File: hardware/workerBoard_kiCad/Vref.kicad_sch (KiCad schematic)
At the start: 10 parts, among them U3 ADR435BRZ, U4 REG103UA-5, U5 ADP7118ARDZ-3.3-R7, U6 ADR4540BRZ

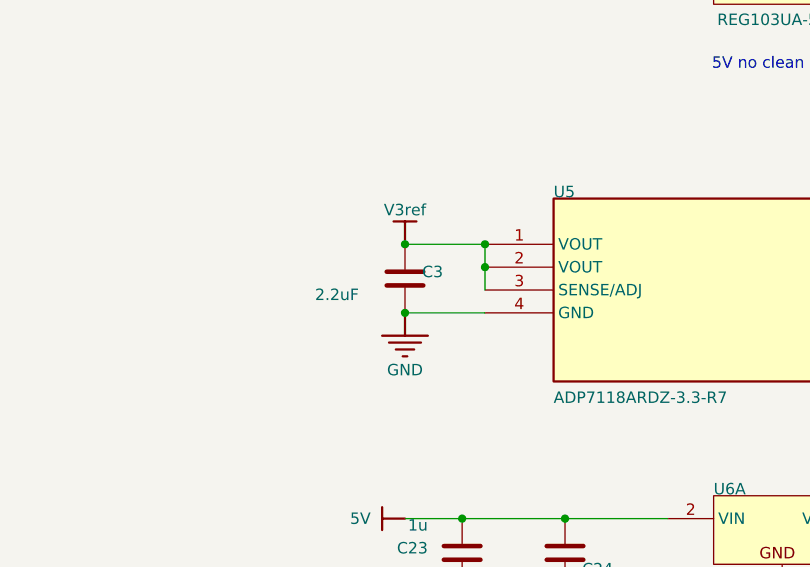
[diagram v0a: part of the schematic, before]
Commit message: Changed worker board layout V2
Removed micro-vias, used only two layers, changed connectors and generally re-worked the worker board
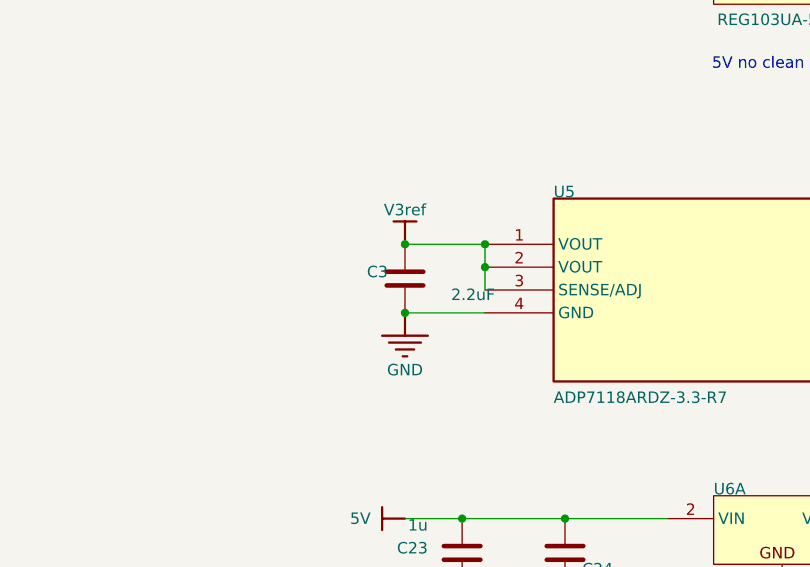
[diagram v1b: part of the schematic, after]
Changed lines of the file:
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@@
     (pin "4")
     (pin "6")
+    (pin "1")
+    (pin "3")
+    (pin "5")
+    (pin "7")
+    (pin "8")
   )
   (symbol (lib_id "Vref-altium-import:GND") (at 135.89 116.84 0) (unit 1)
@@
       (effects (font (size 1.27 1.27)) (justify left bottom) hide)
     )
+    (pin "2")
+    (pin "4")
+    (pin "5")
+    (pin "6")
+    (pin "7")
     (pin "1")
     (pin "3")
@@
     (pin "")
   )
-  (symbol (lib_id "Device:C") (at 135.89 113.03 0) (unit 1)
-    (in_bom yes) (on_board yes)
-    (property "Reference" "C3" (id 0) (at 137.795 113.03 0)
-      (effects (font (size 1.27 1.27)) (justify left bottom))
-    )
-    (property "Value" "2.2uF" (id 1) (at 125.89 115.57 0)
-      (effects (font (size 1.27 1.27)) (justify left bottom))
-    )
-    (property "Footprint" "lib:CAPC1608X90" (id 2) (at 136.8552 116.84 0)
+  (symbol (lib_id "Device:C") (at 135.89 113.03 0) (mirror y) (unit 1)
+    (in_bom yes) (on_board yes)
+    (property "Reference" "C3" (id 0) (at 133.985 113.03 0)
+      (effects (font (size 1.27 1.27)) (justify left bottom))
+    )
+    (property "Value" "2.2uF" (id 1) (at 145.89 115.57 0)
+      (effects (font (size 1.27 1.27)) (justify left bottom))
+    )
+    (property "Footprint" "lib:CAPC1608X90" (id 2) (at 134.9248 116.84 0)
       (effects (font (size 1.27 1.27)) hide)
     )
@@
       (effects (font (size 1.27 1.27)) hide)
     )
-    (property "PACKAGE" "None" (id 4) (at 133.985 107.442 0)
-      (effects (font (size 1.27 1.27)) (justify left bottom) hide)
-    )
-    (property "AVAILABILITY" "Unavailable" (id 5) (at 133.985 107.442 0)
-      (effects (font (size 1.27 1.27)) (justify left bottom) hide)
-    )
-    (property "ALTIUM_VALUE" "*" (id 6) (at 133.985 107.442 0)
-      (effects (font (size 1.27 1.27)) (justify left bottom) hide)
-    )
-    (property "MP" "F981C225MMA" (id 7) (at 133.985 107.442 0)
-      (effects (font (size 1.27 1.27)) (justify left bottom) hide)
-    )
-    (property "PRICE" "None" (id 8) (at 133.985 107.442 0)
-      (effects (font (size 1.27 1.27)) (justify left bottom) hide)
-    )
-    (property "MF" "{'manufacturer': u'AVX'}" (id 9) (at 133.985 107.442 0)
-      (effects (font (size 1.27 1.27)) (justify left bottom) hide)
-    )
-    (property "COMPONENT TYPE" "Standard" (id 10) (at 125.89 107.442 0)
-      (effects (font (size 1.27 1.27)) (justify left bottom) hide)
-    )
-    (property "DESIGN ITEM ID" "F981C225MMA" (id 11) (at 125.89 107.442 0)
-      (effects (font (size 1.27 1.27)) (justify left bottom) hide)
-    )
-    (property "PIN COUNT" "2" (id 12) (at 125.89 107.442 0)
-      (effects (font (size 1.27 1.27)) (justify left bottom) hide)
-    )
-    (property "SOURCE" "workerBoard.SCHLIB" (id 13) (at 125.89 107.442 0)
+    (property "PACKAGE" "None" (id 4) (at 137.795 107.442 0)
+      (effects (font (size 1.27 1.27)) (justify left bottom) hide)
+    )
+    (property "AVAILABILITY" "Unavailable" (id 5) (at 137.795 107.442 0)
+      (effects (font (size 1.27 1.27)) (justify left bottom) hide)
+    )
+    (property "ALTIUM_VALUE" "*" (id 6) (at 137.795 107.442 0)
+      (effects (font (size 1.27 1.27)) (justify left bottom) hide)
+    )
+    (property "MP" "F981C225MMA" (id 7) (at 137.795 107.442 0)
+      (effects (font (size 1.27 1.27)) (justify left bottom) hide)
+    )
+    (property "PRICE" "None" (id 8) (at 137.795 107.442 0)
+      (effects (font (size 1.27 1.27)) (justify left bottom) hide)
+    )
+    (property "MF" "{'manufacturer': u'AVX'}" (id 9) (at 137.795 107.442 0)
+      (effects (font (size 1.27 1.27)) (justify left bottom) hide)
+    )
+    (property "COMPONENT TYPE" "Standard" (id 10) (at 145.89 107.442 0)
+      (effects (font (size 1.27 1.27)) (justify left bottom) hide)
+    )
+    (property "DESIGN ITEM ID" "F981C225MMA" (id 11) (at 145.89 107.442 0)
+      (effects (font (size 1.27 1.27)) (justify left bottom) hide)
+    )
+    (property "PIN COUNT" "2" (id 12) (at 145.89 107.442 0)
+      (effects (font (size 1.27 1.27)) (justify left bottom) hide)
+    )
+    (property "SOURCE" "workerBoard.SCHLIB" (id 13) (at 145.89 107.442 0)
       (effects (font (size 1.27 1.27)) (justify left bottom) hide)
     )
@@
     (pin "6")
     (pin "7")
+    (pin "1")
+    (pin "3")
+    (pin "8")
   )
   (symbol (lib_id "Vref-altium-import:5V") (at 198.12 111.76 90) (unit 1)
@@
       (effects (font (size 1.27 1.27)) (justify left bottom) hide)
     )
+    (pin "2")
+    (pin "4")
+    (pin "6")
     (pin "1")
     (pin "3")

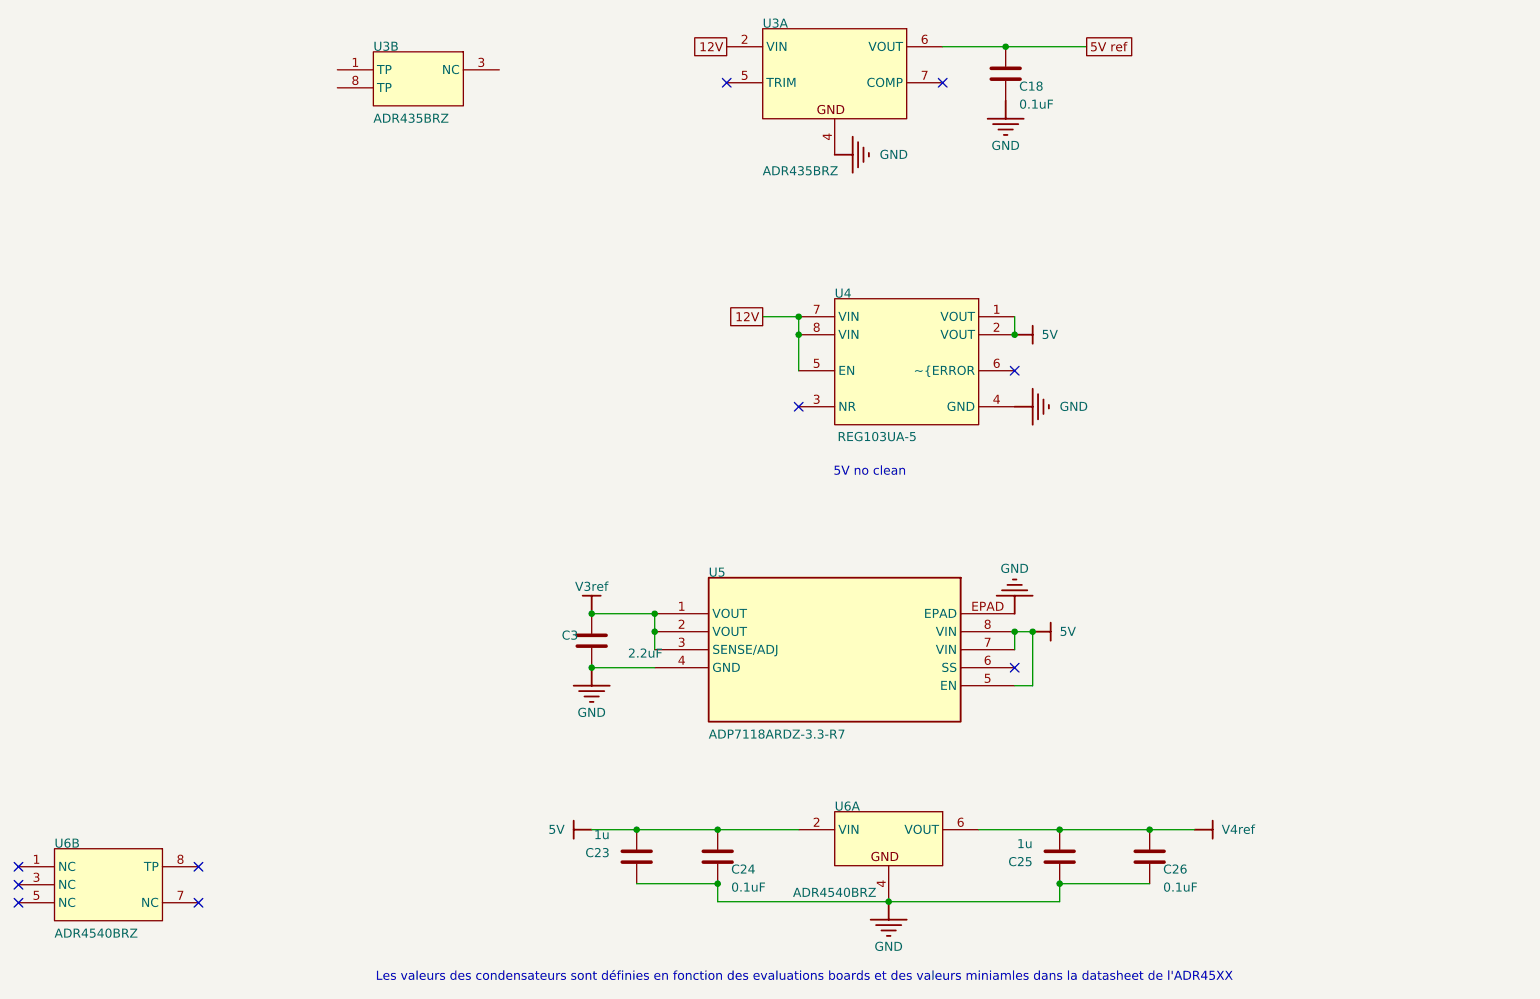
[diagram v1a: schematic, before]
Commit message: Fixed DRC violations
Fixed DRC violations based on missing footprints. Should review THVD8000 foot print as it had to be changed from 'missing' footprint import. This version passes all DRC checks. Net clearance was changed to 0.127 mm (4mill) otherwise the SOT-23 pads were failling DRC
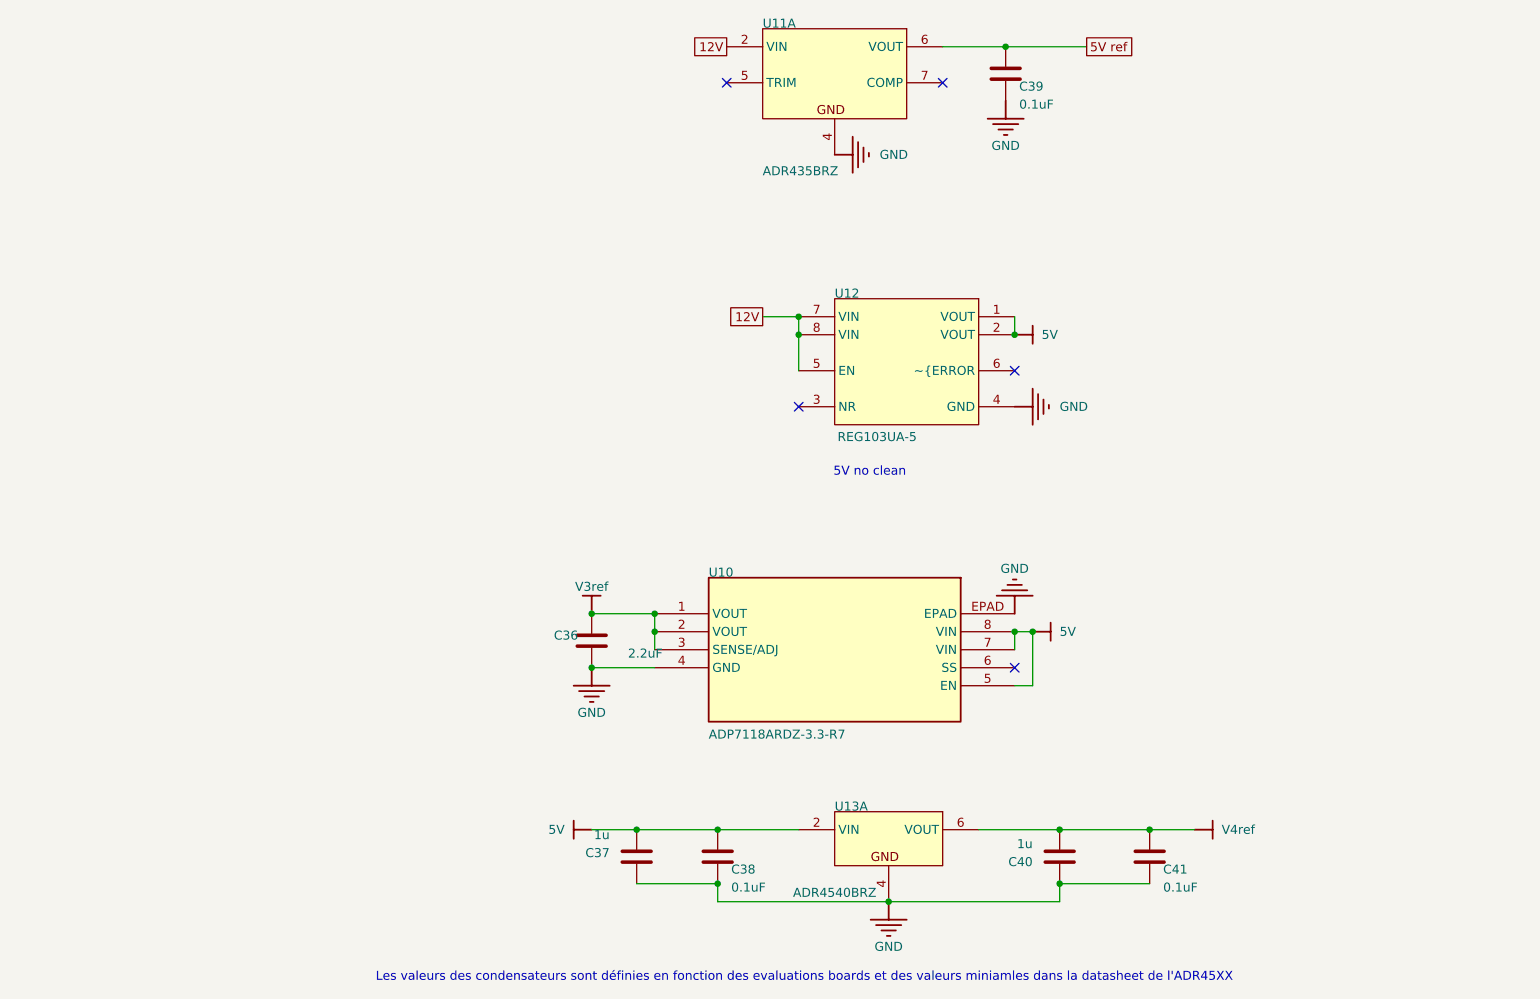
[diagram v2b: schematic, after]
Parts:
- removed unit 2 of U3
- removed unit 2 of U6
- U13: renamed from U6; footprint lib:ADI-R-8_M -> GIGUL-IMPORT:ADI-R-8_M
- renumbered C3 to C36, C23 to C37, C24 to C38, C18 to C39, C25 to C40, C26 to C41, U5 to U10, U3 to U11, U4 to U12
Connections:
- no-connect marks 10 -> 5

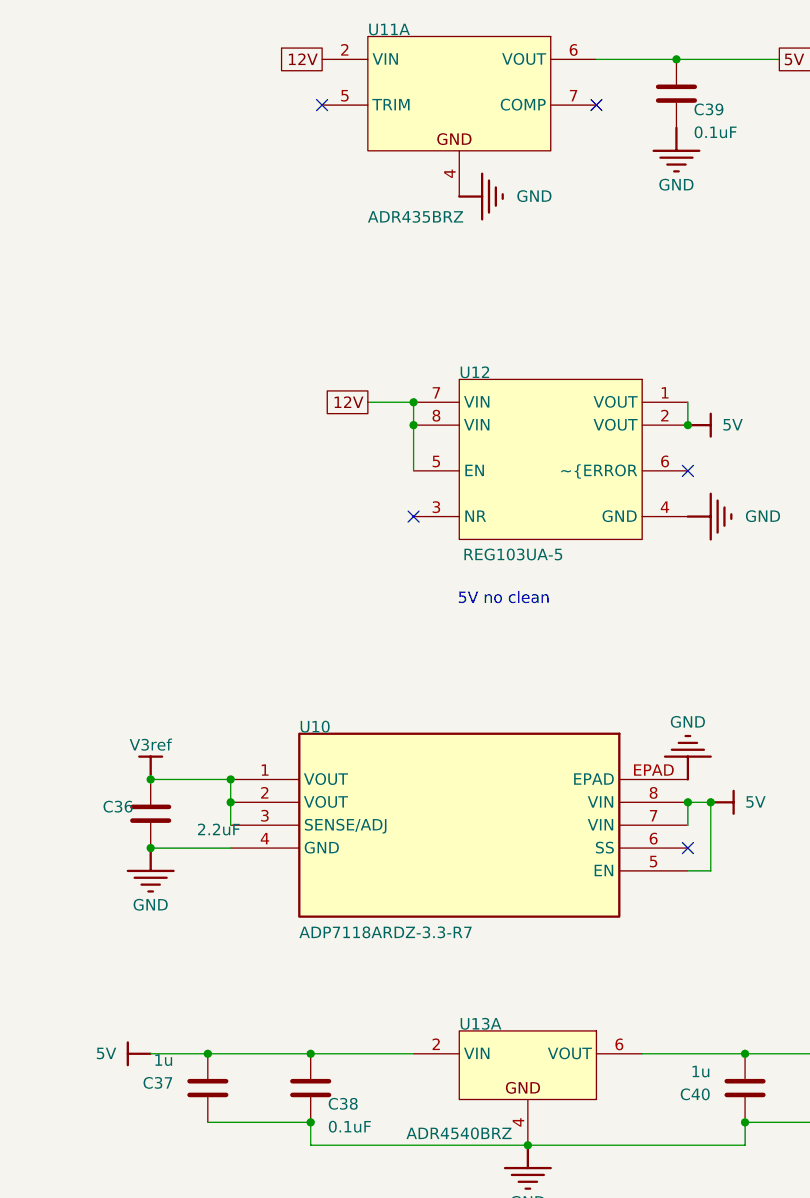
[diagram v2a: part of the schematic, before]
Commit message: Corrected component names to fit with the PCB plan
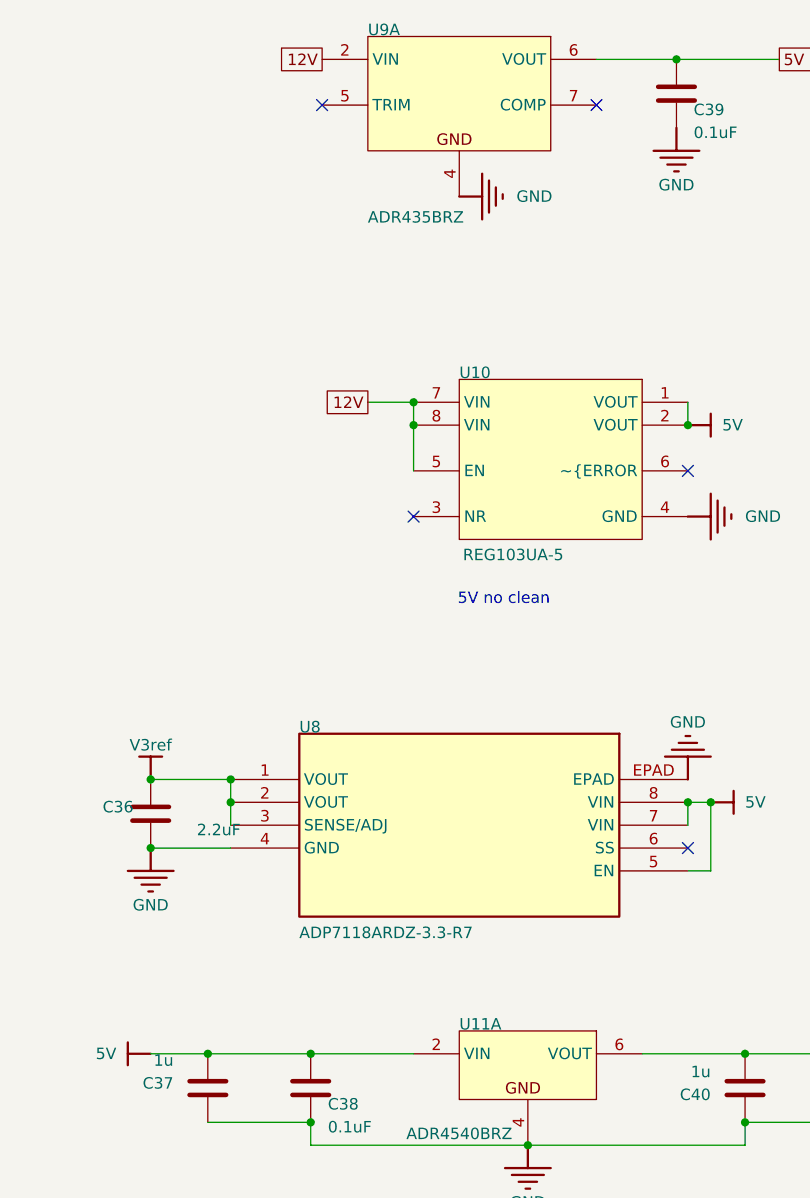
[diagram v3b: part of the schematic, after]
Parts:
- renumbered U12 to U10, U13 to U11, U10 to U8, U11 to U9
